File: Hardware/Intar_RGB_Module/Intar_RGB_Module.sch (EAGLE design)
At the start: 12 parts, among them J2 GROVE-4P-2.0-3470130P1, U1 LP5521LONG

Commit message: Created schematics for first round of modules.
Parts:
- added D1: LED_RGB_6PASMT, Intar_Eagle_Library:LED_RGB_6PASMT
- added R1, R2: 4.7K, SparkFun-Resistors:4.7KOHM-1/10W-1%(0603)
- added R3, R4: 10K, SparkFun-Resistors:10KOHM-1/10W-1%(0603)0603
- added SJ1: (no value), SparkFun-Retired:SOLDERJUMPER_2WAYPASTE1&2&3
- added SJ2, SJ3: (no value), SparkFun-Retired:SOLDERJUMPER_2WAYPASTE2&3
- added U$1: LOGOSM, Intar_Eagle_Library:LOGOSM
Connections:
- new net N$10: R4.1, SJ3.1
- new net N$6: R1.2, SJ1.3
- new net N$7: R2.2, SJ1.1
- new net N$9: R3.1, SJ2.1
- net B: now also D1.B_A
- net G: now also D1.G_A
- net GND: now also D1.B_C, D1.G_C, D1.R_C, SJ2.3, SJ3.3
- net R: now also D1.R_A
- net SCL: now also R2.1
- net SDA: now also R1.1
- net SEL0: now also SJ2.2
- net SEL1: now also SJ3.2
- net VCC: now also R3.2, R4.2, SJ1.2
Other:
- note added: "* Last bit is 0 for write, 1 for read"
- note added: "0110 010x"
- note added: "0110 011x"
- note added: "0110 100x"
- note added: "0110 101x"
- note added: "GND"
- note added: "I2C Addr"
- note added: "I2C Address Selection"
- note added: "RGB LED"
- note added: "SEL0"
- note added: "SEL1"
- note added: "VCC"
- note removed: "* Change R4 and R5 depending on color of D2 and D3"
- note removed: "2.1V"
- note removed: "2.95V"
- note removed: "2V"
- note removed: "51"
- note removed: "56"
- note removed: "6.2"
- note removed: "Blue"
- note removed: "Color"
- note removed: "Green"
- note removed: "R4 & R5"
- note removed: "Red"
- note removed: "Vf"
- note removed: "Visible LED"
- note removed: "Yellow"
- moved on the sheet: J2

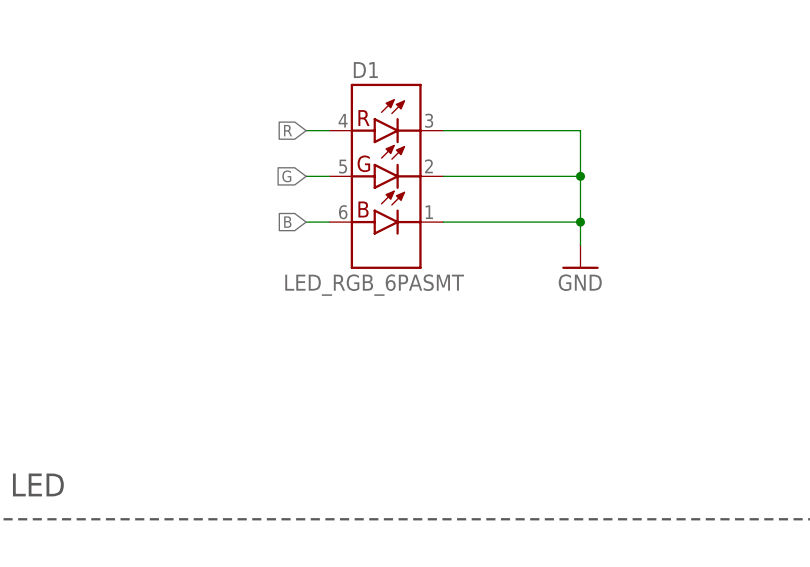
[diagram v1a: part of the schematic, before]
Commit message: Arranged components on all modules
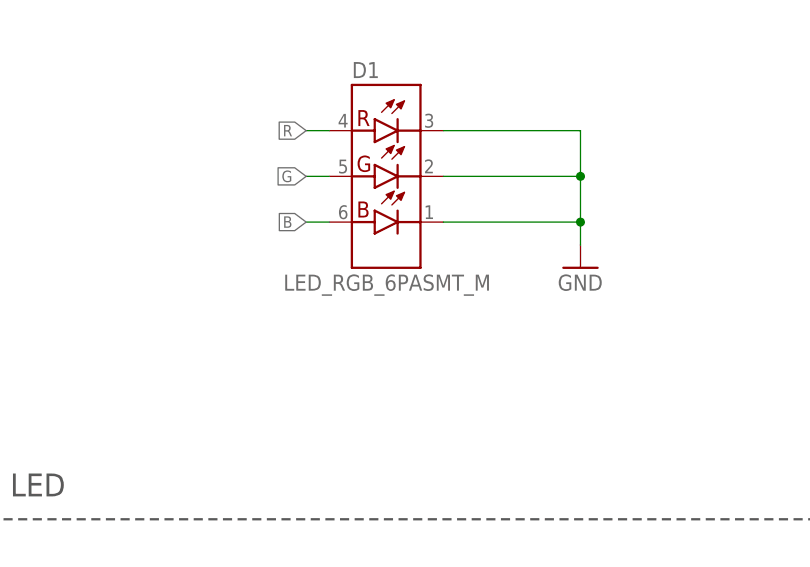
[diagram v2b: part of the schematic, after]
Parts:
- D1: value LED_RGB_6PASMT -> LED_RGB_6PASMT_M; device Intar_Eagle_Library:LED_RGB_6PASMT -> Intar_Eagle_Library:LED_RGB_6PASMT_M
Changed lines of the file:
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@@
 <setting verticaltext="up"/>
 </settings>
-<grid distance="0.1" unitdist="inch" unit="inch" style="lines" multiple="1" display="yes" altdistance="0.01" altunitdist="inch" altunit="inch"/>
+<grid distance="0.1" unitdist="inch" unit="inch" style="lines" multiple="1" display="no" altdistance="0.01" altunitdist="inch" altunit="inch"/>
 <layers>
 <layer number="1" name="Top" color="4" fill="1" visible="no" active="no"/>
@@
 <part name="SJ1" library="SparkFun-Retired" deviceset="SOLDERJUMPER_2WAY" device="PASTE1&amp;2&amp;3"/>
 <part name="SUPPLY3" library="SparkFun-Aesthetics" deviceset="VCC" device=""/>
-<part name="D1" library="Intar_Eagle_Library" deviceset="LED_RGB_6P" device="ASMT"/>
+<part name="D1" library="Intar_Eagle_Library" deviceset="LED_RGB_6P" device="ASMT_M" value="LED_RGB_6PASMT_M"/>
 <part name="GND6" library="SparkFun-Aesthetics" deviceset="GND" device=""/>
 <part name="SJ2" library="SparkFun-Retired" deviceset="SOLDERJUMPER_2WAY" device="PASTE2&amp;3"/>

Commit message: Finished RGB and IR modules
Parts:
- renumbered J2 to J1
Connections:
- net GND: now also J1.4; no longer J1.1
- net SCL: now also J1.1; no longer J1.4
- net SDA: now also J1.2; no longer J1.3
- net VCC: now also J1.3; no longer J1.2
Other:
- note added: "CL"
- note added: "DA"
- note added: "S0"
- note added: "S1"
- note removed: "SCL"
- note removed: "SDA"
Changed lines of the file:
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@@
 <setting verticaltext="up"/>
 </settings>
-<grid distance="0.1" unitdist="inch" unit="inch" style="lines" multiple="1" display="no" altdistance="0.01" altunitdist="inch" altunit="inch"/>
+<grid distance="0.1" unitdist="inch" unit="inch" style="lines" multiple="1" display="yes" altdistance="0.01" altunitdist="inch" altunit="inch"/>
 <layers>
 <layer number="1" name="Top" color="4" fill="1" visible="no" active="no"/>
@@
 <part name="STANDOFF2" library="SparkFun-Electromechanical" deviceset="STAND-OFF" device=""/>
 <part name="LOGO1" library="SparkFun-Aesthetics" deviceset="OSHW-LOGO" device="S"/>
-<part name="J2" library="Connector" deviceset="GROVE-4P-2.0" device="-3470130P1"/>
 <part name="GND5" library="SparkFun-Aesthetics" deviceset="GND" device=""/>
 <part name="SUPPLY5" library="SparkFun-Aesthetics" deviceset="VCC" device=""/>
@@
 <part name="SUPPLY6" library="SparkFun-Aesthetics" deviceset="VCC" device=""/>
 <part name="U$1" library="Intar_Eagle_Library" deviceset="LOGO" device="SM"/>
+<part name="J1" library="Connector" deviceset="GROVE-4P-2.0" device="-3470130P1"/>
 </parts>
 <sheets>
@@
 <text x="49.784" y="144.78" size="1.778" layer="97" align="center-right">G</text>
 <text x="49.784" y="142.24" size="1.778" layer="97" align="center-right">V</text>
-<text x="49.784" y="139.7" size="1.778" layer="97" align="center-right">SDA</text>
-<text x="49.784" y="137.16" size="1.778" layer="97" align="center-right">SCL</text>
+<text x="49.784" y="139.7" size="1.778" layer="97" align="center-right">DA</text>
+<text x="49.784" y="137.16" size="1.778" layer="97" align="center-right">CL</text>
 <wire x1="248.92" y1="106.68" x2="147.32" y2="106.68" width="0.254" layer="97" style="shortdash"/>
 <text x="149.86" y="109.22" size="2.54" layer="97">RGB LED</text>
@@
 <text x="238.76" y="66.04" size="1.778" layer="97" align="bottom-center">0110 101x</text>
 <rectangle x1="89.662" y1="154.432" x2="93.218" y2="155.448" layer="94"/>
-<rectangle x1="167.132" y1="71.12" x2="168.148" y2="72.898" layer="94"/>
-<rectangle x1="195.072" y1="71.12" x2="196.088" y2="72.898" layer="94"/>
+<rectangle x1="167.132" y1="69.342" x2="168.148" y2="71.12" layer="94"/>
+<rectangle x1="195.072" y1="69.342" x2="196.088" y2="71.12" layer="94"/>
+<text x="170.18" y="73.66" size="1.778" layer="97">S1</text>
+<text x="198.12" y="73.66" size="1.778" layer="97">S0</text>
 </plain>
 <instances>
@@
 <instance part="STANDOFF2" gate="G$1" x="241.3" y="27.94"/>
 <instance part="LOGO1" gate="G$1" x="132.08" y="10.16"/>
-<instance part="J2" gate="J" x="53.34" y="140.97" smashed="yes">
-<attribute name="NAME" x="50.8" y="146.812" size="1.27" layer="95" ratio="10"/>
-</instance>
 <instance part="GND5" gate="1" x="66.04" y="147.32"/>
 <instance part="SUPPLY5" gate="G$1" x="73.66" y="144.78"/>
@@
 </instance>
 <instance part="GND6" gate="1" x="220.98" y="134.62"/>
-<instance part="SJ2" gate="G$1" x="195.58" y="71.12"/>
-<instance part="SJ3" gate="G$1" x="167.64" y="71.12"/>
+<instance part="SJ2" gate="G$1" x="195.58" y="71.12" smashed="yes">
+<attribute name="NAME" x="198.12" y="68.58" size="1.778" layer="95"/>
+<attribute name="VALUE" x="198.12" y="69.215" size="1.778" layer="96"/>
+</instance>
+<instance part="SJ3" gate="G$1" x="167.64" y="71.12" smashed="yes">
+<attribute name="NAME" x="170.18" y="68.58" size="1.778" layer="95"/>
+<attribute name="VALUE" x="170.18" y="69.215" size="1.778" layer="96"/>
+</instance>
 <instance part="R3" gate="G$1" x="195.58" y="83.82" smashed="yes" rot="R90">
 <attribute name="NAME" x="198.12" y="86.3346" size="1.778" layer="95"/>
@@
 <instance part="SUPPLY6" gate="G$1" x="167.64" y="91.44"/>
 <instance part="U$1" gate="G$1" x="104.14" y="2.54"/>
+<instance part="J1" gate="J" x="53.34" y="140.97" smashed="yes" rot="MR180">
+<attribute name="NAME" x="50.8" y="146.812" size="1.27" layer="95" ratio="10"/>
+</instance>
 </instances>
 <busses>
@@
 <net name="GND" class="0">
 <segment>
-<pinref part="J2" gate="J" pin="1"/>
 <wire x1="58.42" y1="144.78" x2="60.96" y2="144.78" width="0.1524" layer="91"/>
 <wire x1="60.96" y1="144.78" x2="60.96" y2="152.4" width="0.1524" layer="91"/>
@@
 <wire x1="66.04" y1="152.4" x2="66.04" y2="149.86" width="0.1524" layer="91"/>
 <pinref part="GND5" gate="1" pin="GND"/>
+<pinref part="J1" gate="J" pin="4"/>
 </segment>
 <segment>
@@
 <net name="VCC" class="0">
 <segment>
-<pinref part="J2" gate="J" pin="2"/>
 <wire x1="58.42" y1="142.24" x2="73.66" y2="142.24" width="0.1524" layer="91"/>
 <wire x1="73.66" y1="142.24" x2="73.66" y2="144.78" width="0.1524" layer="91"/>
 <pinref part="SUPPLY5" gate="G$1" pin="VCC"/>
+<pinref part="J1" gate="J" pin="3"/>
 </segment>
 <segment>
@@
 <net name="SDA" class="0">
 <segment>
-<pinref part="J2" gate="J" pin="3"/>
 <wire x1="58.42" y1="139.7" x2="83.82" y2="139.7" width="0.1524" layer="91"/>
 <label x="104.14" y="139.7" size="1.27" layer="95" xref="yes"/>
@@
 <wire x1="83.82" y1="142.24" x2="83.82" y2="139.7" width="0.1524" layer="91"/>
 <junction x="83.82" y="139.7"/>
+<pinref part="J1" gate="J" pin="2"/>
 </segment>
 <segment>
@@
 <net name="SCL" class="0">
 <segment>
-<pinref part="J2" gate="J" pin="4"/>
 <wire x1="58.42" y1="137.16" x2="99.06" y2="137.16" width="0.1524" layer="91"/>
 <label x="104.14" y="137.16" size="1.27" layer="95" xref="yes"/>
@@
 <wire x1="99.06" y1="142.24" x2="99.06" y2="137.16" width="0.1524" layer="91"/>
 <junction x="99.06" y="137.16"/>
-</segment>
-<segment>
+<pinref part="J1" gate="J" pin="1"/>
+</segment>
+<segment>
